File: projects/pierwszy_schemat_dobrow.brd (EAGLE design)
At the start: 100 x 80 mm, 36 parts, among them IC1 74HC595N, IC2 7805T, IC3 LD117AV

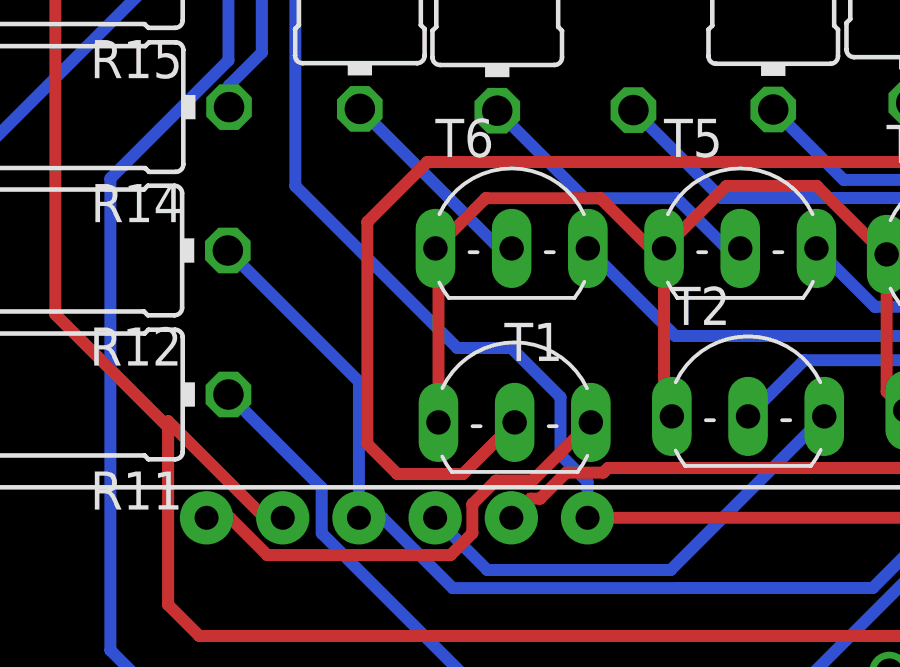
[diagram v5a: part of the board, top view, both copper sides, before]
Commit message: Fixed overlapping circuit
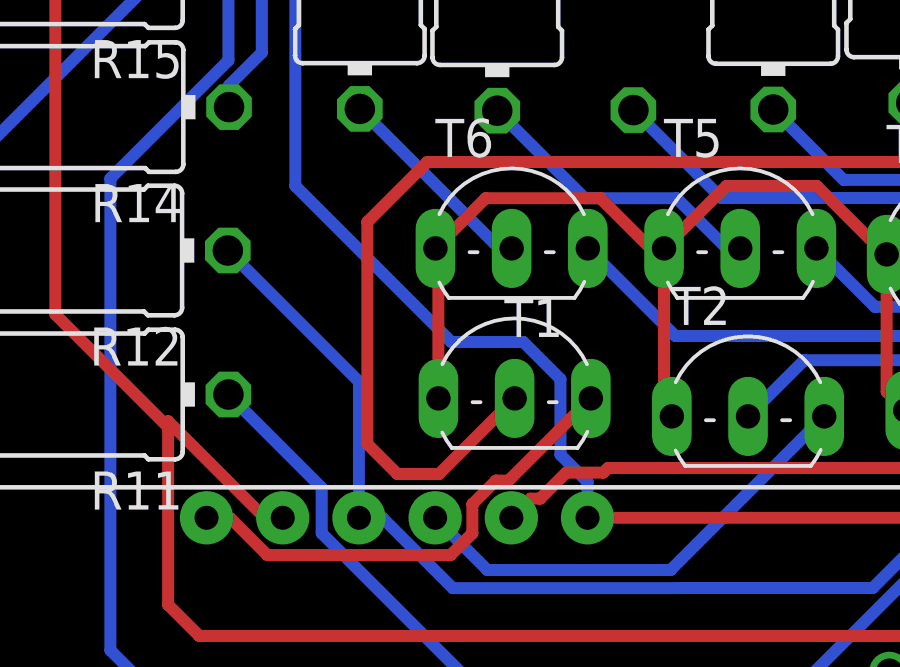
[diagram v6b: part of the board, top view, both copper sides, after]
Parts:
- moved T1 0.80 mm to (40.1, 27.6)
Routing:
- net N$7: track 35.2 -> 34.4 mm
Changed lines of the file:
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@@
 <attribute name="VALUE" x="34.3658" y="47.908" size="1.27" layer="27" ratio="10" rot="R270"/>
 </element>
-<element name="T1" library="transistor" library_urn="urn:adsk.eagle:library:402" package="TO92-EBC" package3d_urn="urn:adsk.eagle:package:29915/2" value="" x="40.11" y="26.79" smashed="yes">
-<attribute name="NAME" x="39.77" y="27.568" size="1.27" layer="25" ratio="10"/>
-<attribute name="POPULARITY" value="0" x="74.4" y="-71" size="1.778" layer="27" display="off"/>
-<attribute name="VALUE" x="37.57" y="22.218" size="1.27" layer="27" ratio="10"/>
+<element name="T1" library="transistor" library_urn="urn:adsk.eagle:library:402" package="TO92-EBC" package3d_urn="urn:adsk.eagle:package:29915/2" value="" x="40.11" y="27.59" smashed="yes">
+<attribute name="NAME" x="39.77" y="28.368" size="1.27" layer="25" ratio="10"/>
+<attribute name="POPULARITY" value="0" x="74.4" y="-70.2" size="1.778" layer="27" display="off"/>
+<attribute name="VALUE" x="37.57" y="23.018" size="1.27" layer="27" ratio="10"/>
 </element>
 <element name="T2" library="transistor" library_urn="urn:adsk.eagle:library:402" package="TO92-EBC" package3d_urn="urn:adsk.eagle:package:29915/2" value="" x="47.89" y="26.99" smashed="yes">
@@
 <wire x1="45.35" y1="25.72" x2="45.09" y2="25.98" width="0.4" layer="1"/>
 <wire x1="45.09" y1="25.98" x2="45.09" y2="31.32" width="0.4" layer="1"/>
-<wire x1="37.57" y1="25.52" x2="37.57" y2="31.22" width="0.4" layer="1"/>
+<wire x1="37.57" y1="26.32" x2="37.57" y2="31.22" width="0.4" layer="1"/>
 <wire x1="37.57" y1="31.22" x2="37.47" y2="31.32" width="0.4" layer="1"/>
 <wire x1="44.64271875" y1="31.32" x2="45.09" y2="31.32" width="0.4" layer="1"/>
@@
 <wire x1="37.2" y1="34.2" x2="35.2" y2="32.2" width="0.4" layer="1"/>
 <wire x1="35.2" y1="24.8" x2="36.2" y2="23.8" width="0.4" layer="1"/>
-<wire x1="36.2" y1="23.8" x2="38.39" y2="23.8" width="0.4" layer="1"/>
-<wire x1="38.39" y1="23.8" x2="40.11" y2="25.52" width="0.4" layer="1"/>
+<wire x1="36.2" y1="23.8" x2="37.59" y2="23.8" width="0.4" layer="1"/>
+<wire x1="37.59" y1="23.8" x2="40.11" y2="26.32" width="0.4" layer="1"/>
 <wire x1="35.2" y1="32.2" x2="35.2" y2="24.8" width="0.4" layer="1"/>
 </signal>
@@
 <wire x1="30.55" y1="45.63" x2="32.8" y2="43.38" width="0.4" layer="16"/>
 <wire x1="32.8" y1="43.38" x2="32.8" y2="33.4" width="0.4" layer="16"/>
-<wire x1="32.8" y1="33.4" x2="38.2" y2="28" width="0.4" layer="16"/>
-<wire x1="38.2" y1="28" x2="40" y2="28" width="0.4" layer="16"/>
-<wire x1="40" y1="28" x2="41.6372" y2="26.3628" width="0.4" layer="16"/>
-<wire x1="41.6372" y1="26.3628" x2="41.6372" y2="24.44008125" width="0.4" layer="16"/>
+<wire x1="32.8" y1="33.4" x2="38" y2="28.2" width="0.4" layer="16"/>
+<wire x1="38" y1="28.2" x2="40.4" y2="28.2" width="0.4" layer="16"/>
+<wire x1="40.4" y1="28.2" x2="41.6372" y2="26.9628" width="0.4" layer="16"/>
+<wire x1="41.6372" y1="26.9628" x2="41.6372" y2="24.44008125" width="0.4" layer="16"/>
 <wire x1="42.54" y1="23.53728125" x2="42.54" y2="22.34" width="0.4" layer="16"/>
 <wire x1="41.6372" y1="24.44008125" x2="42.54" y2="23.53728125" width="0.4" layer="16"/>
@@
 <contactref element="LED1" pad="12"/>
 <wire x1="38.7014" y1="21.82579375" x2="37.97420625" y2="21.0986" width="0.4" layer="1"/>
-<wire x1="42.65" y1="25.52" x2="40.7114" y2="23.5814" width="0.4" layer="1"/>
+<wire x1="42.65" y1="26.32" x2="39.9114" y2="23.5814" width="0.4" layer="1"/>
 <wire x1="30.62439375" y1="22.34" x2="29.84" y2="22.34" width="0.4" layer="1"/>
-<wire x1="40.7114" y1="23.5814" x2="39.48579375" y2="23.5814" width="0.4" layer="1"/>
+<wire x1="39.9114" y1="23.5814" x2="39.48579375" y2="23.5814" width="0.4" layer="1"/>
 <wire x1="31.86579375" y1="21.0986" x2="30.62439375" y2="22.34" width="0.4" layer="1"/>
 <wire x1="39.48579375" y1="23.5814" x2="38.7014" y2="22.79700625" width="0.4" layer="1"/>

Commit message: Update pierwszy_schemat_dobrow.brd
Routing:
- net SEG_A: track 98.9 -> 104.0 mm
- net N$2: track 33.1 -> 36.1 mm
- net DATA_PIN: track 74.9 -> 76.2 mm
- net VCC_5V: track 160.3 -> 161.2 mm
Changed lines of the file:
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@@
 <attribute name="POPULARITY" value="65" x="129.6" y="-14.2" size="1.778" layer="27" display="off"/>
 <attribute name="SPICEPREFIX" value="C" x="129.6" y="-14.2" size="1.778" layer="27" display="off"/>
-<attribute name="VALUE" x="63.814" y="41.426" size="1.27" layer="27" ratio="10"/>
+<attribute name="VALUE" x="65.414" y="45.826" size="1.27" layer="27" ratio="10"/>
 </element>
 <element name="C4" library="rcl" library_urn="urn:adsk.eagle:library:334" package="C025-025X050" package3d_urn="urn:adsk.eagle:package:23629/2" value="10u" x="66.05" y="38.78" smashed="yes" rot="R180">
@@
 <attribute name="POPULARITY" value="65" x="-3.8" y="97.2" size="1.778" layer="27" rot="R180" display="off"/>
 <attribute name="SPICEPREFIX" value="C" x="-3.8" y="97.2" size="1.778" layer="27" rot="R180" display="off"/>
-<attribute name="VALUE" x="68.336" y="41.574" size="1.27" layer="27" ratio="10" rot="R180"/>
+<attribute name="VALUE" x="67.936" y="36.974" size="1.27" layer="27" ratio="10" rot="R180"/>
 </element>
 <element name="C5" library="rcl" library_urn="urn:adsk.eagle:library:334" package="C025-025X050" package3d_urn="urn:adsk.eagle:package:23629/2" value="0.1u" x="61.62" y="41.4" smashed="yes" rot="R270">
@@
 <attribute name="POPULARITY" value="65" x="3.2" y="-34.8" size="1.778" layer="27" rot="R270" display="off"/>
 <attribute name="SPICEPREFIX" value="C" x="3.2" y="-34.8" size="1.778" layer="27" rot="R270" display="off"/>
-<attribute name="VALUE" x="58.826" y="43.686" size="1.27" layer="27" ratio="10" rot="R270"/>
+<attribute name="VALUE" x="63.026" y="43.486" size="1.27" layer="27" ratio="10" rot="R270"/>
 </element>
 <element name="D1" library="7SEG-vertical" package="7SEG-13" package3d_urn="urn:adsk.eagle:package:26668/2" value="" x="67.13" y="14.76" smashed="yes">
@@
 <attribute name="POPULARITY" value="0" x="-34.2" y="109" size="1.778" layer="27" rot="R180" display="off"/>
 <attribute name="SPICEPREFIX" value="R" x="-34.2" y="109" size="1.778" layer="27" rot="R180" display="off"/>
-<attribute name="VALUE" x="21.468" y="26.8342" size="1.27" layer="27" ratio="10" rot="R180"/>
+<attribute name="VALUE" x="27.268" y="27.2342" size="1.27" layer="27" ratio="10" rot="R180"/>
 </element>
 <element name="R12" library="rcl" library_urn="urn:adsk.eagle:library:334" package="0414/15" package3d_urn="urn:adsk.eagle:package:23579/2" value="220" x="22.93" y="31.25" smashed="yes" rot="R180">
@@
 <attribute name="POPULARITY" value="0" x="-35.4" y="-31.4" size="1.778" layer="27" rot="R270" display="off"/>
 <attribute name="SPICEPREFIX" value="R" x="-35.4" y="-31.4" size="1.778" layer="27" rot="R270" display="off"/>
-<attribute name="VALUE" x="38.3458" y="45.048" size="1.27" layer="27" ratio="10" rot="R270"/>
+<attribute name="VALUE" x="38.1458" y="48.048" size="1.27" layer="27" ratio="10" rot="R270"/>
 </element>
 <element name="R9" library="rcl" library_urn="urn:adsk.eagle:library:334" package="0414/15" package3d_urn="urn:adsk.eagle:package:23579/2" value="100" x="34.95" y="43.59" smashed="yes" rot="R270">
@@
 <wire x1="63.41" y1="76.14" x2="76.12" y2="76.14" width="0.5" layer="16"/>
 <wire x1="76.12" y1="76.14" x2="83.2" y2="69.06" width="0.5" layer="16"/>
-<wire x1="61.62" y1="42.67" x2="63.17" y2="44.22" width="0.5" layer="16"/>
-<wire x1="63.17" y1="44.22" x2="64.83" y2="44.22" width="0.5" layer="16"/>
+<wire x1="61.62" y1="42.67" x2="61.62" y2="44.22" width="0.5" layer="16"/>
+<wire x1="61.62" y1="44.22" x2="64.83" y2="44.22" width="0.5" layer="16"/>
 <wire x1="63.41" y1="76.14" x2="55.87" y2="68.6" width="0.5" layer="16"/>
 <wire x1="23.3" y1="68.6" x2="20.74" y2="71.16" width="0.5" layer="16"/>
@@
 <contactref element="R5" pad="2"/>
 <wire x1="57.4484" y1="37.2244" x2="58.3716" y2="37.2244" width="0.4" layer="1"/>
-<wire x1="58.3716" y1="37.2244" x2="62.6" y2="32.996" width="0.4" layer="1"/>
+<wire x1="58.3716" y1="37.2244" x2="65" y2="30.596" width="0.4" layer="1"/>
 <wire x1="53.33" y1="36.17" x2="56.394" y2="36.17" width="0.4" layer="1"/>
 <wire x1="56.394" y1="36.17" x2="57.4484" y2="37.2244" width="0.4" layer="1"/>
-<via x="62.4" y="27" extent="1-16" drill="0.9"/>
-<wire x1="62.4" y1="27" x2="59.22271875" y2="27" width="0.4" layer="16"/>
-<wire x1="59.22271875" y1="27" x2="58.62951875" y2="27.5932" width="0.4" layer="16"/>
+<via x="64.6" y="27.2" extent="1-16" drill="0.9"/>
+<wire x1="64.6" y1="27.2" x2="59.02271875" y2="27.2" width="0.4" layer="16"/>
+<wire x1="59.02271875" y1="27.2" x2="58.62951875" y2="27.5932" width="0.4" layer="16"/>
 <wire x1="58.62951875" y1="27.5932" x2="49.7632" y2="27.5932" width="0.4" layer="16"/>
 <wire x1="49.7632" y1="27.5932" x2="47.89" y2="25.72" width="0.4" layer="16"/>
-<wire x1="62.6" y1="32.996" x2="62.6" y2="27.2" width="0.4" layer="1"/>
-<wire x1="62.6" y1="27.2" x2="62.4" y2="27" width="0.4" layer="1"/>
+<wire x1="65" y1="30.596" x2="65" y2="27.6" width="0.4" layer="1"/>
+<wire x1="65" y1="27.6" x2="64.6" y2="27.2" width="0.4" layer="1"/>
 </signal>
 <signal name="N$3">
@@
 <contactref element="U$1" pad="D12"/>
 <contactref element="IC1" pad="14"/>
-<wire x1="35.98" y1="71.16" x2="32.7196" y2="74.4204" width="0.4" layer="1"/>
-<wire x1="32.7196" y1="74.4204" x2="7.7508" y2="74.4204" width="0.4" layer="1"/>
-<wire x1="7.7508" y1="74.4204" x2="1.5224" y2="68.192" width="0.4" layer="1"/>
-<wire x1="1.5224" y1="68.192" x2="1.5224" y2="35.4576" width="0.4" layer="1"/>
+<wire x1="35.98" y1="71.16" x2="31.3196" y2="75.8204" width="0.4" layer="1"/>
+<wire x1="31.3196" y1="75.8204" x2="8.9508" y2="75.8204" width="0.4" layer="1"/>
+<wire x1="8.9508" y1="75.8204" x2="1.5224" y2="68.392" width="0.4" layer="1"/>
+<wire x1="1.5224" y1="68.392" x2="1.5224" y2="35.4576" width="0.4" layer="1"/>
 <wire x1="1.5224" y1="35.4576" x2="4.19" y2="32.79" width="0.4" layer="1"/>
 </signal>
@@
 <contactref element="IC1" pad="12"/>
 <wire x1="41.06" y1="71.16" x2="37.62" y2="74.6" width="0.4" layer="16"/>
-<wire x1="8.2" y1="74.6" x2="1.8" y2="68.2" width="0.4" layer="16"/>
-<wire x1="1.8" y1="68.2" x2="1.8" y2="40.26" width="0.4" layer="16"/>
-<wire x1="1.8" y1="40.26" x2="4.19" y2="37.87" width="0.4" layer="16"/>
-<wire x1="37.62" y1="74.6" x2="8.2" y2="74.6" width="0.4" layer="16"/>
+<wire x1="8.4" y1="74.6" x2="2" y2="68.2" width="0.4" layer="16"/>
+<wire x1="2" y1="68.2" x2="2" y2="40.06" width="0.4" layer="16"/>
+<wire x1="2" y1="40.06" x2="4.19" y2="37.87" width="0.4" layer="16"/>
+<wire x1="37.62" y1="74.6" x2="8.4" y2="74.6" width="0.4" layer="16"/>
 </signal>
 <signal name="SEG_G">
@@
 <wire x1="30.61" y1="50.41" x2="28.21" y2="50.41" width="0.4" layer="1"/>
 <wire x1="28.21" y1="50.41" x2="24.8" y2="47" width="0.4" layer="1"/>
-<wire x1="24.8" y1="47" x2="24.8" y2="29.12" width="0.4" layer="1"/>
+<wire x1="24.8" y1="29.32" x2="24.8" y2="29.12" width="0.4" layer="1"/>
 <wire x1="31.78" y1="22.34" x2="32.38" y2="22.34" width="0.4" layer="1"/>
-<wire x1="31.78" y1="22.34" x2="28.56" y2="25.56" width="0.4" layer="1"/>
+<wire x1="31.78" y1="22.34" x2="24.8" y2="29.32" width="0.4" layer="1"/>
 <wire x1="28.56" y1="25.36" x2="24.8" y2="29.12" width="0.4" layer="1"/>
 <wire x1="69.67" y1="22.38" x2="65.69" y2="18.4" width="0.4" layer="1"/>
@@
 <wire x1="29.6" y1="18.4" x2="28.56" y2="19.44" width="0.4" layer="1"/>
 <wire x1="28.56" y1="19.44" x2="28.56" y2="25.36" width="0.4" layer="1"/>
-<wire x1="28.56" y1="25.36" x2="28.56" y2="25.56" width="0.4" layer="1"/>
+<wire x1="24.8" y1="47" x2="24.8" y2="29.32" width="0.4" layer="1"/>
 </signal>
 <signal name="SEG_B">
@@
 <contactref element="LED1" pad="12"/>
 <wire x1="38.7014" y1="21.82579375" x2="37.97420625" y2="21.0986" width="0.4" layer="1"/>
-<wire x1="42.65" y1="26.32" x2="39.9114" y2="23.5814" width="0.4" layer="1"/>
+<wire x1="42.65" y1="26.32" x2="42.22439375" y2="26.32" width="0.4" layer="1"/>
+<wire x1="42.22439375" y1="26.32" x2="38.7014" y2="22.79700625" width="0.4" layer="1"/>
 <wire x1="30.62439375" y1="22.34" x2="29.84" y2="22.34" width="0.4" layer="1"/>
-<wire x1="39.9114" y1="23.5814" x2="39.48579375" y2="23.5814" width="0.4" layer="1"/>
 <wire x1="31.86579375" y1="21.0986" x2="30.62439375" y2="22.34" width="0.4" layer="1"/>
-<wire x1="39.48579375" y1="23.5814" x2="38.7014" y2="22.79700625" width="0.4" layer="1"/>
 <wire x1="38.7014" y1="22.79700625" x2="38.7014" y2="21.82579375" width="0.4" layer="1"/>
 <wire x1="37.97420625" y1="21.0986" x2="31.86579375" y2="21.0986" width="0.4" layer="1"/>
@@
 <wire x1="40" y1="22.34" x2="40.6382" y2="22.9782" width="0.4" layer="1"/>
 <wire x1="40.6382" y1="22.9782" x2="40.96125625" y2="22.9782" width="0.4" layer="1"/>
-<wire x1="43.06951875" y1="23.8468" x2="43.22271875" y2="24" width="0.4" layer="1"/>
-<wire x1="43.22271875" y1="24" x2="57" y2="24" width="0.4" layer="1"/>
-<wire x1="40.96125625" y1="22.9782" x2="41.82985625" y2="23.8468" width="0.4" layer="1"/>
-<wire x1="41.82985625" y1="23.8468" x2="43.06951875" y2="23.8468" width="0.4" layer="1"/>
+<wire x1="40.96125625" y1="22.9782" x2="41.98305625" y2="24" width="0.4" layer="1"/>
+<wire x1="41.98305625" y1="24" x2="57" y2="24" width="0.4" layer="1"/>
 <wire x1="57" y1="24" x2="58.21" y2="25.21" width="0.4" layer="1"/>
 <wire x1="58.21" y1="25.21" x2="58.21" y2="25.92" width="0.4" layer="1"/>

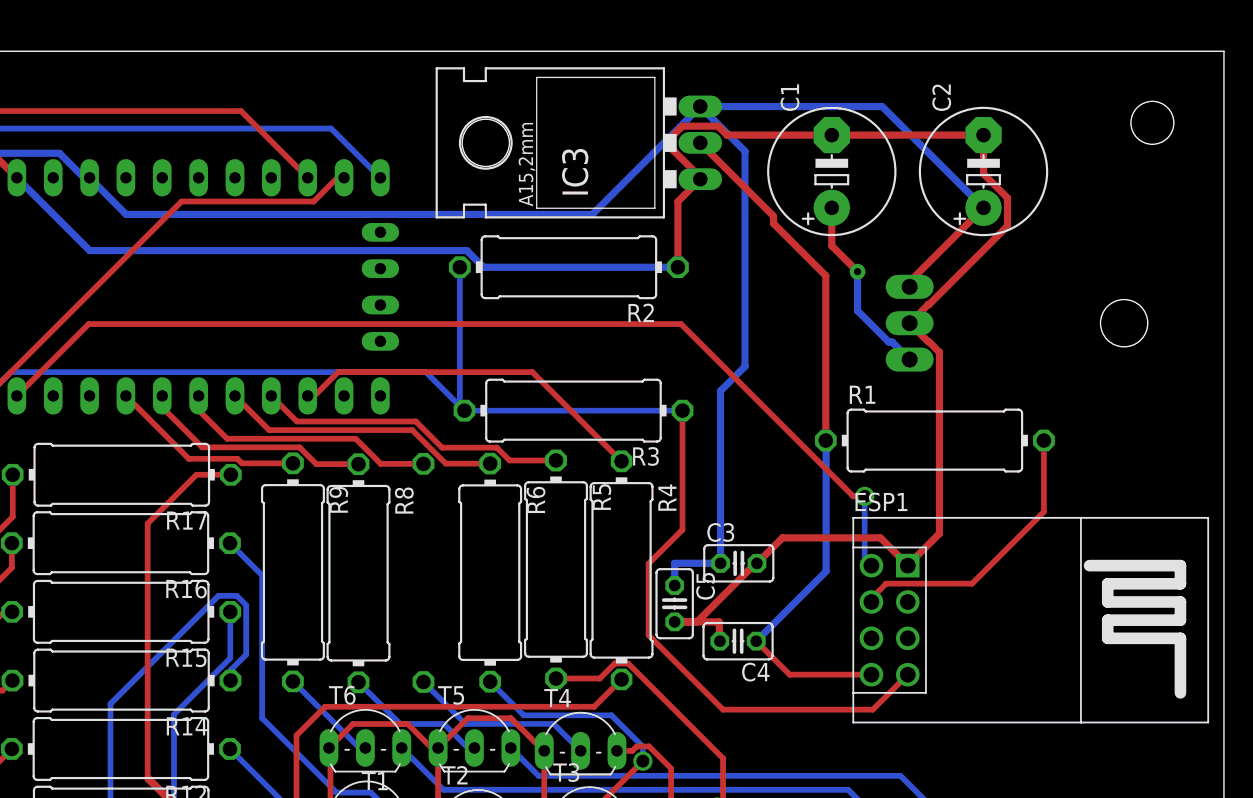
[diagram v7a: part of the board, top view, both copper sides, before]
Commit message: Added power jack
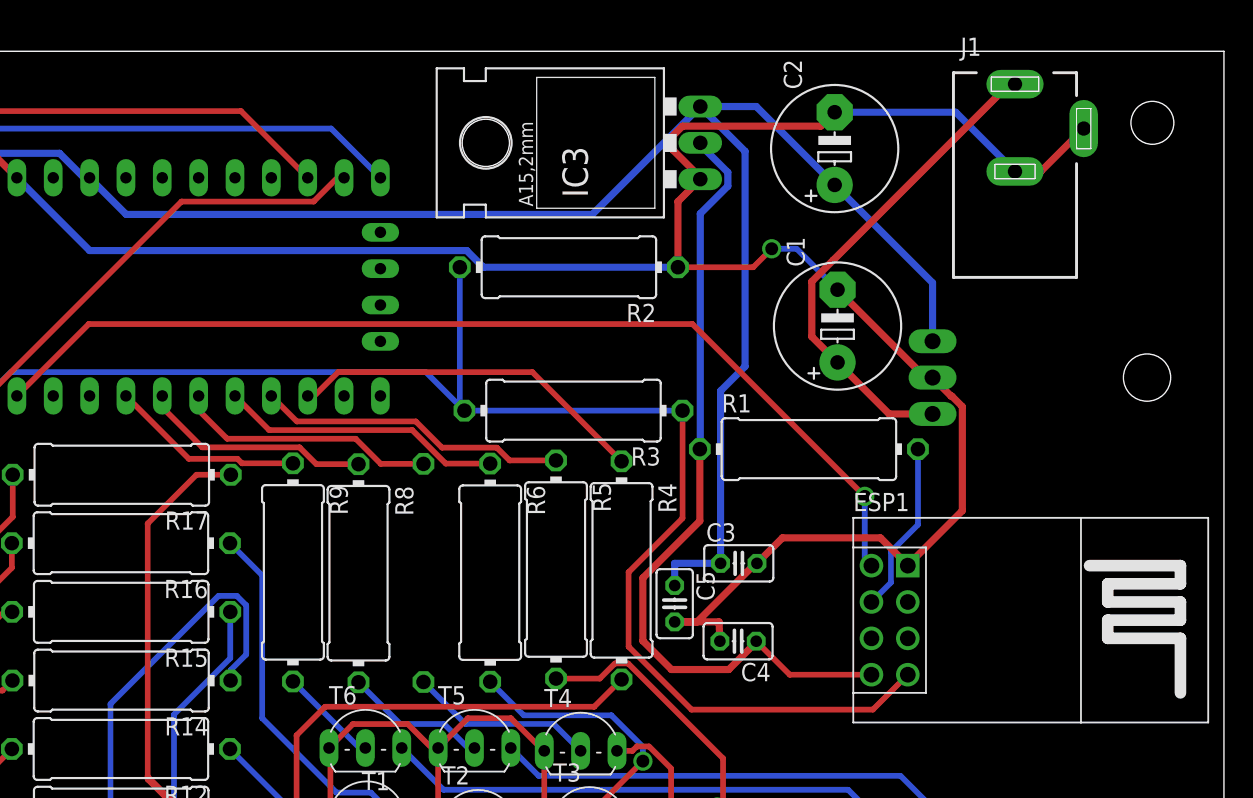
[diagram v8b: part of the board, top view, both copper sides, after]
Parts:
- added J1: DCJ0202, con-jack:DCJ0202
- moved C1 10.8 mm to (73.0, 60.8)
- moved C2 10.5 mm to (72.8, 73.2)
- moved R1 8.82 mm to (71.0, 52.2)
- moved IC2 4.12 mm to (89.8, 57.2)
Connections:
- net GND: now also J1.2, J1.3
- net VIN_9V: now also J1.1
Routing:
- net VIN_9V: track 13.0 -> 34.4 mm, vias 1 -> 0
- net GND: track 204.6 -> 217.5 mm, vias 0 -> 1
- net N$10: track 19.8 -> 12.0 mm
- net VCC_3V3: track 49.5 -> 56.7 mm
- net VCC_5V: track 161.2 -> 156.3 mm
- net TX_ARDUINO: track 99.4 -> 101.8 mm
